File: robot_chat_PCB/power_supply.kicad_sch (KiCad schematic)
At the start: 32 parts, among them J301 Conn_01x02, SW301 SW_SPDT_MSM, U301 MP1475DJ-LF-P, U302 MIC5317-3.3xM5

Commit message: Mise à jour placement
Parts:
- +3V301: value TestPoint -> 3.3V
- +5V301: value TestPoint -> 5V
- C302, C303, C305: footprint Capacitor_SMD:C_0603_1608Metric -> Capacitor_SMD:C_0402_1005Metric
- D301: value LED_Small -> 5V
- D304: value LED_Small -> 3.3V
- J301: value Conn_01x02 -> Bat
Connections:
- net +3.3V: now also R309.2; no longer D304.2 (A)
- net GND: now also D304.1 (K); no longer R309.1
- new net: D304.2 (A), R309.1
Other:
- moved on the sheet: R309
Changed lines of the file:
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@@
       (effects (font (size 1.27 1.27)) (justify left))
     )
-    (property "Footprint" "Capacitor_SMD:C_0603_1608Metric" (at 69.85 128.27 0)
+    (property "Footprint" "Capacitor_SMD:C_0402_1005Metric" (at 69.85 128.27 0)
       (effects (font (size 1.27 1.27)) hide)
     )
@@
     (in_bom yes) (on_board yes) (dnp no)
     (property "Reference" "D301" (at 63.5 153.67 0)
-      (effects (font (size 1.27 1.27)))
-    )
-    (property "Value" "LED_Small" (at 63.4365 154.94 0)
-      (effects (font (size 1.27 1.27)) hide)
+      (effects (font (size 1.27 1.27)) hide)
+    )
+    (property "Value" "5V" (at 63.5 153.67 0)
+      (effects (font (size 1.27 1.27)))
     )
     (property "Footprint" "LED_SMD:LED_0603_1608Metric" (at 63.5 151.13 90)
@@
     )
   )
-  (symbol (lib_id "Device:LED_Small") (at 252.73 135.89 270) (mirror x) (unit 1)
-    (in_bom yes) (on_board yes) (dnp no)
-    (property "Reference" "D304" (at 255.27 137.0965 90)
-      (effects (font (size 1.27 1.27)) (justify left))
-    )
-    (property "Value" "LED_Small" (at 255.27 134.5565 90)
-      (effects (font (size 1.27 1.27)) (justify left))
-    )
-    (property "Footprint" "LED_SMD:LED_0603_1608Metric" (at 252.73 135.89 90)
-      (effects (font (size 1.27 1.27)) hide)
-    )
-    (property "Datasheet" "~" (at 252.73 135.89 90)
+  (symbol (lib_id "Device:LED_Small") (at 246.38 144.78 0) (mirror x) (unit 1)
+    (in_bom yes) (on_board yes) (dnp no)
+    (property "Reference" "D304" (at 245.1735 147.32 90)
+      (effects (font (size 1.27 1.27)) (justify left) hide)
+    )
+    (property "Value" "3.3V" (at 246.38 147.32 90)
+      (effects (font (size 1.27 1.27)) (justify left))
+    )
+    (property "Footprint" "LED_SMD:LED_0603_1608Metric" (at 246.38 144.78 90)
+      (effects (font (size 1.27 1.27)) hide)
+    )
+    (property "Datasheet" "~" (at 246.38 144.78 90)
       (effects (font (size 1.27 1.27)) hide)
     )
@@
   )
   (symbol (lib_id "Connector_Generic:Conn_01x02") (at 57.15 53.34 0) (mirror y) (unit 1)
-    (in_bom yes) (on_board yes) (dnp no) (fields_autoplaced)
+    (in_bom yes) (on_board yes) (dnp no)
     (property "Reference" "J301" (at 54.61 53.34 0)
-      (effects (font (size 1.27 1.27)) (justify left))
-    )
-    (property "Value" "Conn_01x02" (at 54.61 55.88 0)
+      (effects (font (size 1.27 1.27)) (justify left) hide)
+    )
+    (property "Value" "Bat" (at 54.61 54.61 0)
       (effects (font (size 1.27 1.27)) (justify left))
     )
@@
     (in_bom yes) (on_board yes) (dnp no)
     (property "Reference" "+3V301" (at 257.81 124.46 0)
-      (effects (font (size 1.27 1.27)) (justify left))
-    )
-    (property "Value" "TestPoint" (at 256.54 126.238 0)
       (effects (font (size 1.27 1.27)) (justify left) hide)
     )
+    (property "Value" "3.3V" (at 259.08 123.19 0)
+      (effects (font (size 1.27 1.27)) (justify left))
+    )
     (property "Footprint" "TestPoint:TestPoint_Pad_D1.0mm" (at 254 128.27 0)
       (effects (font (size 1.27 1.27)) hide)
@@
       (effects (font (size 1.27 1.27)) (justify left))
     )
-    (property "Footprint" "Capacitor_SMD:C_0603_1608Metric" (at 67.31 142.24 0)
+    (property "Footprint" "Capacitor_SMD:C_0402_1005Metric" (at 67.31 142.24 0)
       (effects (font (size 1.27 1.27)) hide)
     )
@@
     (in_bom yes) (on_board yes) (dnp no)
     (property "Reference" "+5V301" (at 165.1 147.32 0)
-      (effects (font (size 1.27 1.27)) (justify left))
-    )
-    (property "Value" "TestPoint" (at 166.37 145.542 0)
       (effects (font (size 1.27 1.27)) (justify left) hide)
+    )
+    (property "Value" "5V" (at 162.56 148.59 0)
+      (effects (font (size 1.27 1.27)) (justify left))
     )
     (property "Footprint" "TestPoint:TestPoint_Pad_D1.0mm" (at 168.91 143.51 0)
@@
     )
   )
-  (symbol (lib_id "Device:R_Small") (at 246.38 144.78 90) (unit 1)
-    (in_bom yes) (on_board yes) (dnp no) (fields_autoplaced)
-    (property "Reference" "R309" (at 246.38 139.7 90)
-      (effects (font (size 1.27 1.27)))
-    )
-    (property "Value" "1k" (at 246.38 142.24 90)
-      (effects (font (size 1.27 1.27)))
-    )
-    (property "Footprint" "Resistor_SMD:R_0603_1608Metric" (at 246.38 144.78 0)
-      (effects (font (size 1.27 1.27)) hide)
-    )
-    (property "Datasheet" "~" (at 246.38 144.78 0)
+  (symbol (lib_id "Device:R_Small") (at 252.73 135.89 180) (unit 1)
+    (in_bom yes) (on_board yes) (dnp no) (fields_autoplaced)
+    (property "Reference" "R309" (at 255.27 134.62 0)
+      (effects (font (size 1.27 1.27)) (justify right))
+    )
+    (property "Value" "1k" (at 255.27 137.16 0)
+      (effects (font (size 1.27 1.27)) (justify right))
+    )
+    (property "Footprint" "Resistor_SMD:R_0603_1608Metric" (at 252.73 135.89 0)
+      (effects (font (size 1.27 1.27)) hide)
+    )
+    (property "Datasheet" "~" (at 252.73 135.89 0)
       (effects (font (size 1.27 1.27)) hide)
     )
@@
       (effects (font (size 1.27 1.27)) (justify left))
     )
-    (property "Footprint" "Capacitor_SMD:C_0603_1608Metric" (at 119.38 139.7 0)
-      (effects (font (size 1.27 1.27)) hide)
-    )
+    (property "Footprint" "Capacitor_SMD:C_0402_1005Metric" (at 119.38 139.7 0)
+      (effects (font (size 1.27 1.27)) hide)
+    )

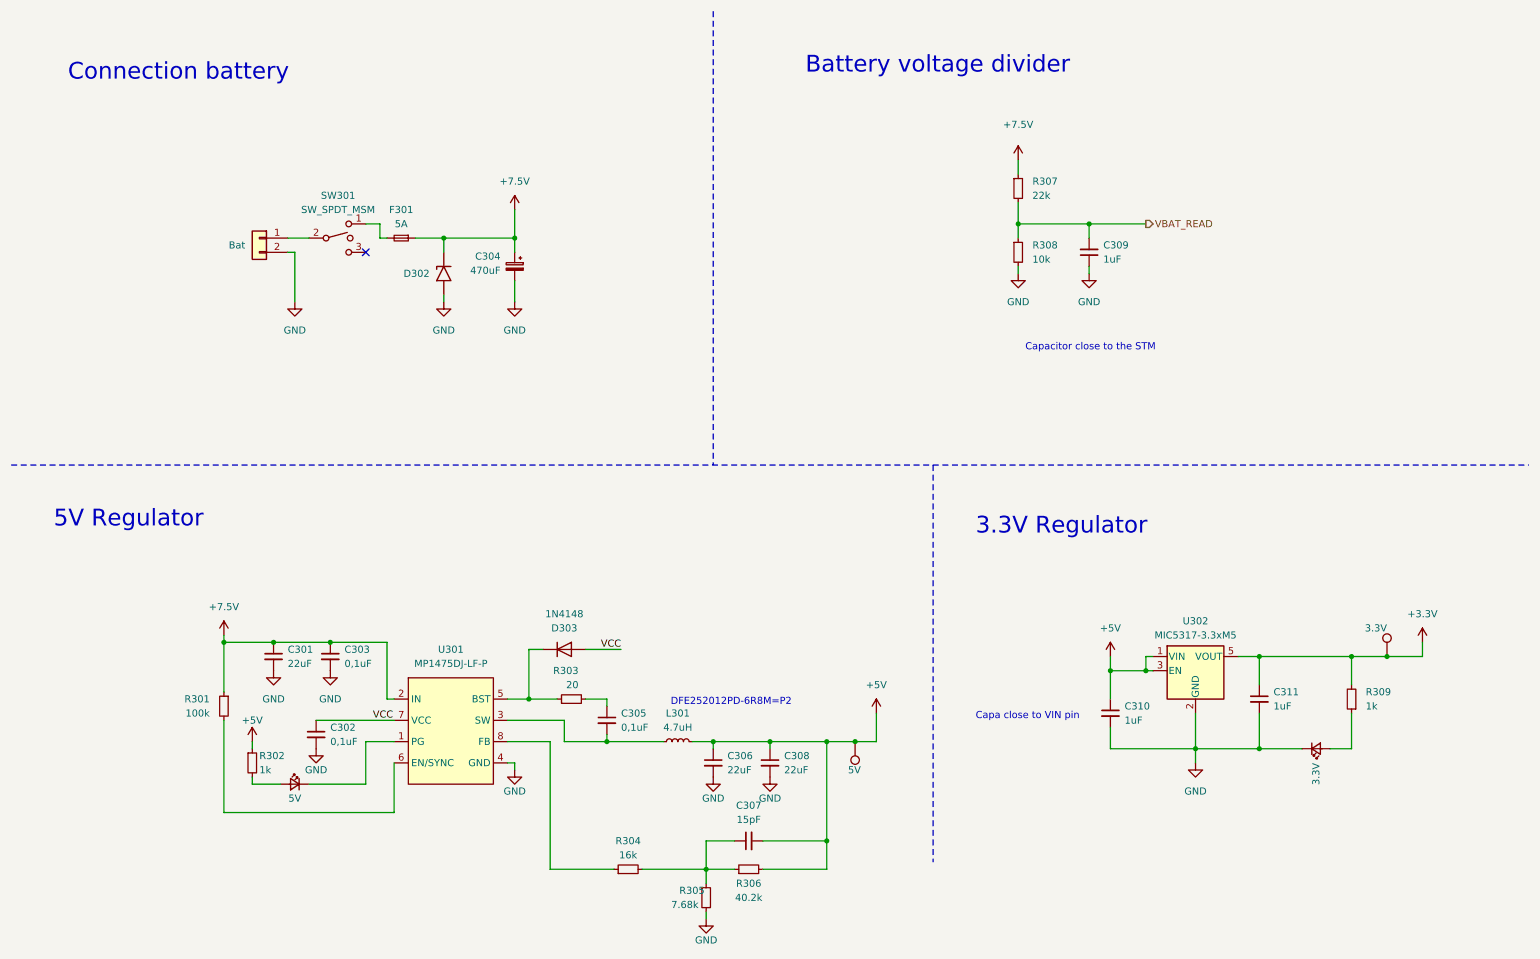
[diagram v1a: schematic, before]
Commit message: changed Rsense position
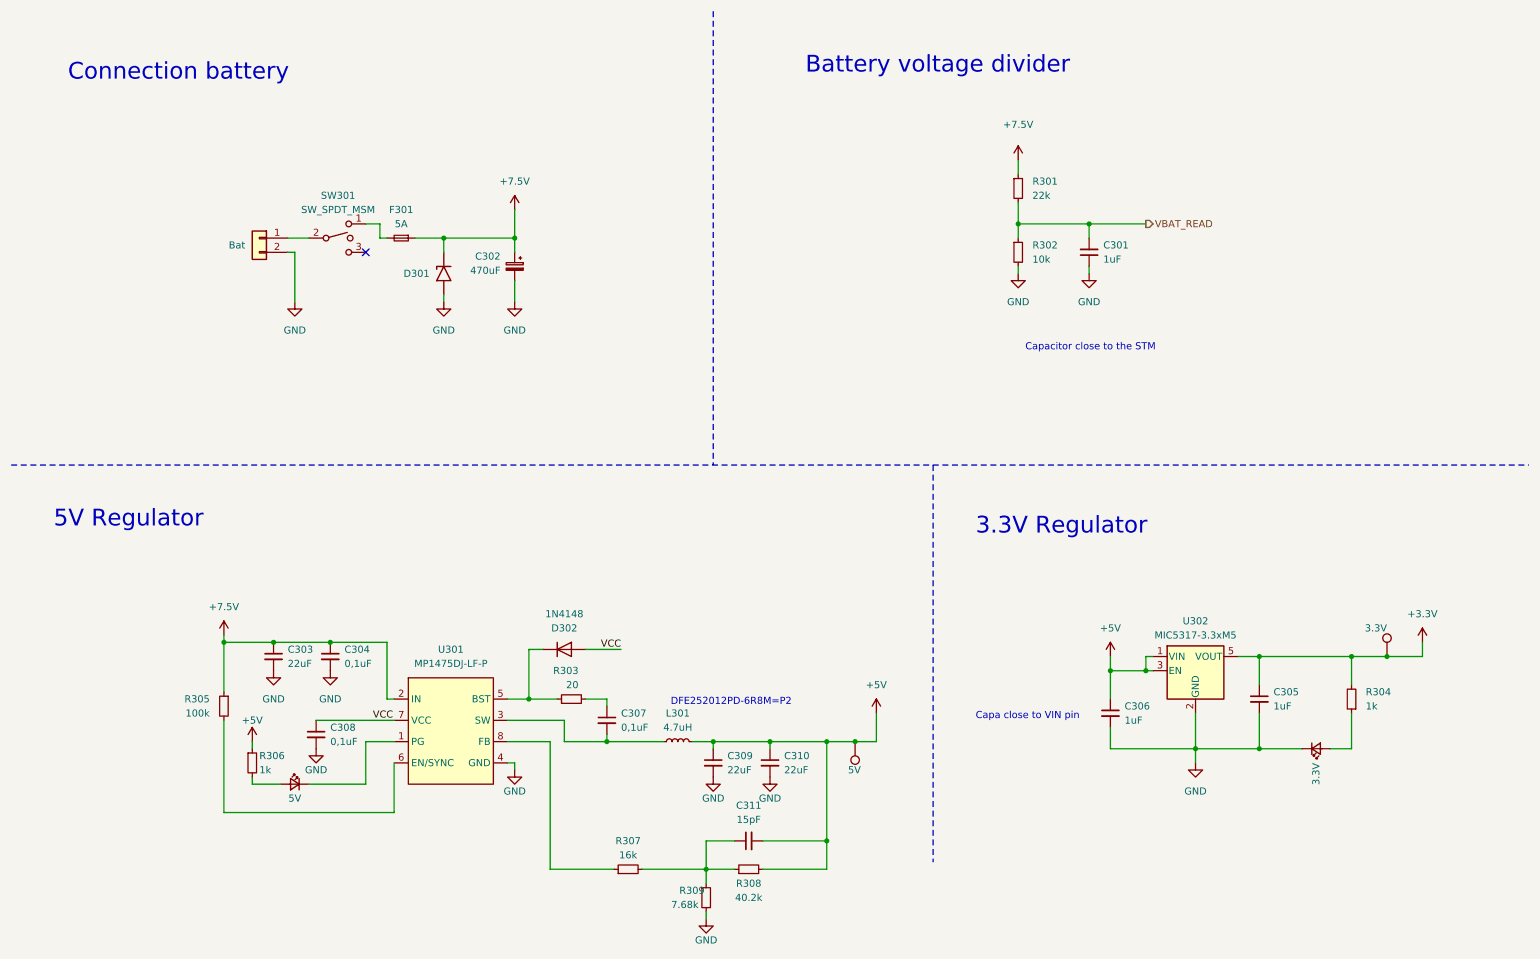
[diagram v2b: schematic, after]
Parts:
- renumbered C309 to C301, C304 to C302, C301 to C303, C303 to C304, C311 to C305, C310 to C306, C305 to C307, C302 to C308, C306 to C309, C308 to C310, C307 to C311, D302 to D301, D303 to D302, D304 to D303, D301 to D304, R307 to R301, R308 to R302, R309 to R304, R301 to R305, R302 to R306, R304 to R307, R306 to R308, R305 to R309

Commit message: Routage final v1.2
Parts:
- F301: value 5A -> 10A; footprint Fuse:Fuse_0603_1608Metric -> Fuse:Fuse_1206_3216Metric
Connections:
- net PG: now reaches D304.1 (K), U301.1 (PG)
- net EN/SYNC: now reaches R305.2, U301.6 (EN/SYNC)
- net BST: now reaches D302.1 (K), R303.1, U301.5 (BST)
- net SW: now reaches C307.2, L301.1, U301.3 (SW)
- net FB: now reaches R307.1, U301.8 (FB)
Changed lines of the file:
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@@
     (effects (font (size 3 3)) (justify left bottom))
+  )
+  (label "EN{slash}SYNC" (at 80.01 156.21 180) (fields_autoplaced)
+    (effects (font (size 1.27 1.27)) (justify right bottom))
   )
   (label "VCC" (at 77.47 139.7 0) (fields_autoplaced)
@@
     (effects (font (size 1.27 1.27)) (justify right bottom))
   )
+  (label "FB" (at 101.6 143.51 0) (fields_autoplaced)
+    (effects (font (size 1.27 1.27)) (justify left bottom))
+  )
+  (label "PG" (at 81.28 143.51 180) (fields_autoplaced)
+    (effects (font (size 1.27 1.27)) (justify right bottom))
+  )
+  (label "BST" (at 101.6 135.89 0) (fields_autoplaced)
+    (effects (font (size 1.27 1.27)) (justify left bottom))
+  )
+  (label "SW" (at 101.6 139.7 0) (fields_autoplaced)
+    (effects (font (size 1.27 1.27)) (justify left bottom))
+  )
   (hierarchical_label "VBAT_READ" (shape output) (at 215.9 50.8 0) (fields_autoplaced)
     (effects (font (size 1.27 1.27)) (justify left))
@@
       (effects (font (size 1.27 1.27)))
     )
-    (property "Value" "5A" (at 82.55 50.8 0)
-      (effects (font (size 1.27 1.27)))
-    )
-    (property "Footprint" "Fuse:Fuse_0603_1608Metric" (at 82.55 53.34 0)
+    (property "Value" "10A" (at 82.55 50.8 0)
+      (effects (font (size 1.27 1.27)))
+    )
+    (property "Footprint" "Fuse:Fuse_1206_3216Metric" (at 82.55 53.34 0)
       (effects (font (size 1.27 1.27)) hide)
     )
@@
   (symbol (lib_id "Device:R_Small") (at 137.16 171.45 0) (unit 1)
     (in_bom yes) (on_board yes) (dnp no)
-    (property "Reference" "R309" (at 134.62 170.18 0)
-      (effects (font (size 1.27 1.27)))
-    )
+    (property "Reference" "R309" (at 133.35 170.18 0)
+      (effects (font (size 1.27 1.27)))
+    )

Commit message: fixed DRC, added html bom
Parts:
- D301: Farnell Part Number (none) -> 3373187RL
- D303, D304: Farnell Part Number (none) -> 3796304
- F301: Farnell Part Number (none) -> 3564732
- J301: Farnell Part Number (none) -> 1516289
- SW301: Farnell Part Number (none) -> 4244949
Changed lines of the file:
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@@
+      (effects (font (size 1.27 1.27)) hide)
+    )
+    (property "Farnell Part Number" "3796304" (at 63.5 151.13 0)
       (effects (font (size 1.27 1.27)) hide)
     )
@@
       (effects (font (size 1.27 1.27)) hide)
     )
+    (property "Farnell Part Number" "3796304" (at 246.38 144.78 90)
+      (effects (font (size 1.27 1.27)) hide)
+    )
     (pin "1")
     (pin "2")
@@
       (effects (font (size 1.27 1.27)) hide)
     )
+    (property "Farnell Part Number" "1516289" (at 57.15 53.34 0)
+      (effects (font (size 1.27 1.27)) hide)
+    )
     (pin "1")
     (pin "2")
@@
     )
     (property "Datasheet" "~" (at 82.55 53.34 0)
+      (effects (font (size 1.27 1.27)) hide)
+    )
+    (property "Farnell Part Number" "3564732" (at 82.55 53.34 0)
       (effects (font (size 1.27 1.27)) hide)
     )
@@
       (effects (font (size 1.27 1.27)) hide)
     )
+    (property "Farnell Part Number" "3373187RL" (at 90.17 59.69 90)
+      (effects (font (size 1.27 1.27)) hide)
+    )
     (pin "1")
     (pin "2")
@@
       (effects (font (size 1.27 1.27)) hide)
     )
+    (property "Farnell Part Number" "4244949" (at 71.12 53.34 0)
+      (effects (font (size 1.27 1.27)) hide)
+    )
